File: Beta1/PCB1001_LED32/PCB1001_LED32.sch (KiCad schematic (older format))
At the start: 148 parts, among them U0 APA102C, U1 APA102C, U10 APA102C, U11 APA102C, U12 APA102C, U13 APA102C, U14 APA102C, U15 APA102C, U16 APA102C, U17 APA102C, U18 APA102C, U19 APA102C, U2 APA102C, U20 APA102C, U21 APA102C, U22 APA102C, U23 APA102C, U24 APA102C, U25 APA102C, U26 APA102C, U27 APA102C, U28 APA102C, U29 APA102C, U3 APA102C, U30 APA102C, U31 APA102C, U4 APA102C, U5 APA102C, U6 APA102C, U7 APA102C, U8 APA102C, U9 APA102C

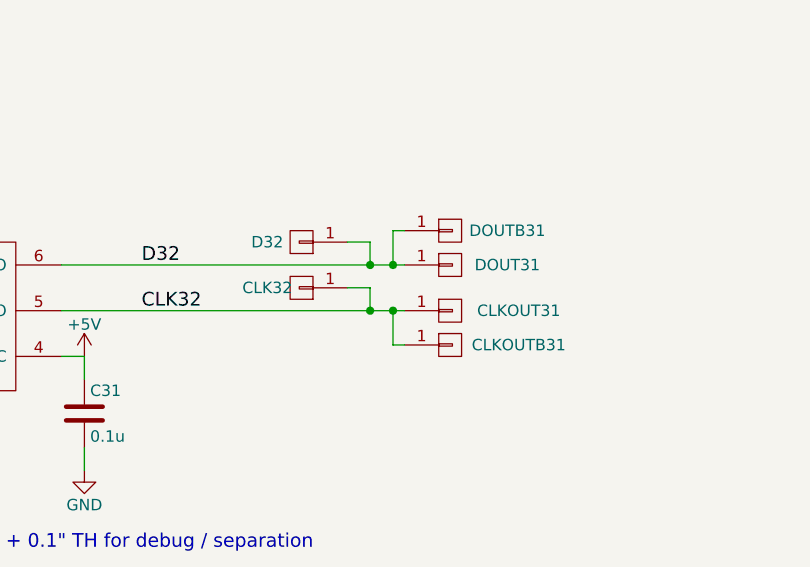
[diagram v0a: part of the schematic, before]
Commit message: Mid reroute. Move interference. Clean silk.
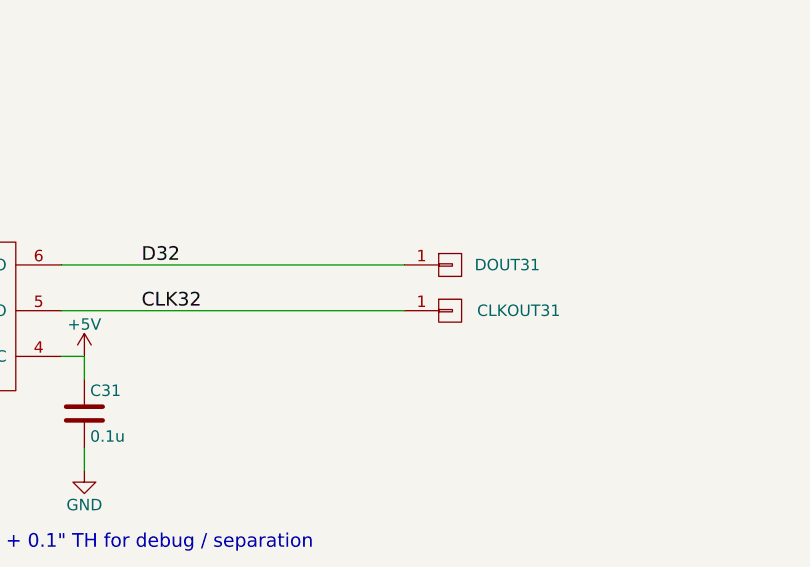
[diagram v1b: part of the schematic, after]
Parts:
- removed CLK32, D32: CONN_01X01, Liberry:TESTPAD, symbol CONN_01X01
- removed CLKOUTB31, DOUTB31: CONN_01X01, Liberry:single_0.1, symbol CONN_01X01
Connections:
- wire segments 315 -> 307
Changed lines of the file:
@@
 LIBS:Zilog
 LIBS:believotron_wanderlust
+LIBS:PCB1001_LED32-cache
 EELAYER 25 0
 EELAYER END
@@
 CLK16
 $Comp
-L CONN_01X01 D32
-U 1 1 5838361B
-P 27500 8950
-F 0 "D32" H 27650 8950 50  0000 C CNN
-F 1 "CONN_01X01" V 27600 8950 50  0001 C CNN
-F 2 "Liberry:TESTPAD" H 23300 4750 50  0001 C CNN
-F 3 "" H 27500 8950 50  0000 C CNN
-F 4 "PCB" H 27500 8950 60  0001 C CNN "MFG"
-F 5 "ON_PCB" H 27500 8950 60  0001 C CNN "MPN"
-	1    27500 8950
-	-1   0    0    1
-$EndComp
-$Comp
-L CONN_01X01 CLK32
-U 1 1 58383624
-P 27500 9150
-F 0 "CLK32" H 27650 9150 50  0000 C CNN
-F 1 "CONN_01X01" V 27600 9150 50  0001 C CNN
-F 2 "Liberry:TESTPAD" H 23300 4750 50  0001 C CNN
-F 3 "" H 27500 9150 50  0000 C CNN
-F 4 "PCB" H 27500 9150 60  0001 C CNN "MFG"
-F 5 "ON_PCB" H 27500 9150 60  0001 C CNN "MPN"
-	1    27500 9150
-	-1   0    0    1
-$EndComp
-$Comp
 L SN74LV1T125DBVR UCLK0
 U 1 1 582E5237
@@
 $EndComp
 $Comp
-L CONN_01X01 DOUTB31
-U 1 1 58311E0F
-P 28150 8900
-F 0 "DOUTB31" H 28400 8900 50  0000 C CNN
-F 1 "CONN_01X01" V 28250 8900 50  0001 C CNN
-F 2 "Liberry:single_0.1" H 28150 8900 50  0001 C CNN
-F 3 "" H 28150 8900 50  0000 C CNN
-F 4 "PCB" H 28150 8900 60  0001 C CNN "MFG"
-F 5 "ON_PCB" H 28150 8900 60  0001 C CNN "MPN"
-	1    28150 8900
-	1    0    0    -1
-$EndComp
-$Comp
-L CONN_01X01 CLKOUTB31
-U 1 1 58312577
-P 28150 9400
-F 0 "CLKOUTB31" H 28450 9400 50  0000 C CNN
-F 1 "CONN_01X01" V 28250 9400 50  0001 C CNN
-F 2 "Liberry:single_0.1" H 28150 9400 50  0001 C CNN
-F 3 "" H 28150 9400 50  0000 C CNN
-F 4 "PCB" H 28150 9400 60  0001 C CNN "MFG"
-F 5 "ON_PCB" H 28150 9400 60  0001 C CNN "MPN"
-	1    28150 9400
-	1    0    0    -1
-$EndComp
-$Comp
 L CONN_01X01 DB16
 U 1 1 5832C873
@@
 Connection ~ 9450 6550
 Wire Wire Line
-	27700 9150 27800 9150
-Wire Wire Line
-	27800 9150 27800 9250
-Connection ~ 27800 9250
-Wire Wire Line
-	27700 8950 27800 8950
-Wire Wire Line
-	27800 8950 27800 9050
-Connection ~ 27800 9050
-Wire Wire Line
 	3800 1050 3800 1250
 Wire Wire Line
@@
 Connection ~ 9050 1150
 Wire Wire Line
-	27950 8900 27900 8900
-Wire Wire Line
-	27900 8900 27900 9050
-Connection ~ 27900 9050
-Wire Wire Line
-	27950 9400 27900 9400
-Wire Wire Line
-	27900 9400 27900 9250
-Connection ~ 27900 9250
-Wire Wire Line
 	8900 6200 9000 6200

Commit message: Changed from 36U to 38U. Ready for Fab.
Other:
- note added: "2017-03-31"
- note added: "Author: Dazzling Duke of Lazers"
- note added: "Believotron Wanderlust 32 CH RGB LED PCB"
- note added: "DATE"
- note added: "Files and Open source MIT License: github.com/Believotron/BelievotronWanderlustHardware\nMarketing Pap: Believotron.com\nThe good stuff: community.believotron.com"
- note added: "Short CS to +5V on downstream daisy chained PCBs."
- note removed: "LED strip, APA102C x 8, + 0.1" TH for debug / separation"
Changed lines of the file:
@@
 	1    0    0    -1
 $EndComp
-Text Notes 30000 19050 0    60   ~ 0
-LED strip, APA102C x 8, + 0.1" TH for debug / separation
 Text Label 17500 1150 0    60   ~ 0
 D4
@@
 	1    0    0    -1
 $EndComp
-Text Notes 25200 10300 0    60   ~ 0
-LED strip, APA102C x 8, + 0.1" TH for debug / separation
 Text Label 26850 6350 0    60   ~ 0
 D24
@@
 Wire Wire Line
 	24350 6550 25450 6550
+Text Notes 29300 20700 0    60   ~ 0
+Files and Open source MIT License: github.com/Believotron/BelievotronWanderlustHardware\nMarketing Pap: Believotron.com\nThe good stuff: community.believotron.com
+Text Notes 29650 21250 0    60   ~ 0
+Believotron Wanderlust 32 CH RGB LED PCB
+Text Notes 30500 21350 0    60   ~ 0
+2017-03-31
+Text Notes 32850 21350 0    60   ~ 0
+DATE
+Text Notes 29300 20800 0    60   ~ 0
+Author: Dazzling Duke of Lazers
+Text Notes 1200 2650 0    60   ~ 0
+Short CS to +5V on downstream daisy chained PCBs.
 $EndSCHEMATC
